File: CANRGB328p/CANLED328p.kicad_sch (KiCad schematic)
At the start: 30 parts, among them J1 Conn_01x06_Socket, J2 Conn_01x03_Socket, J3 AVR-ISP-6, U1 MCP2515-I_SO, U2 TSR_1-2450, U3 MCP2561-E_SN, U4 ATmega328-P, Y1 16 MHz, Y2 8 MHz

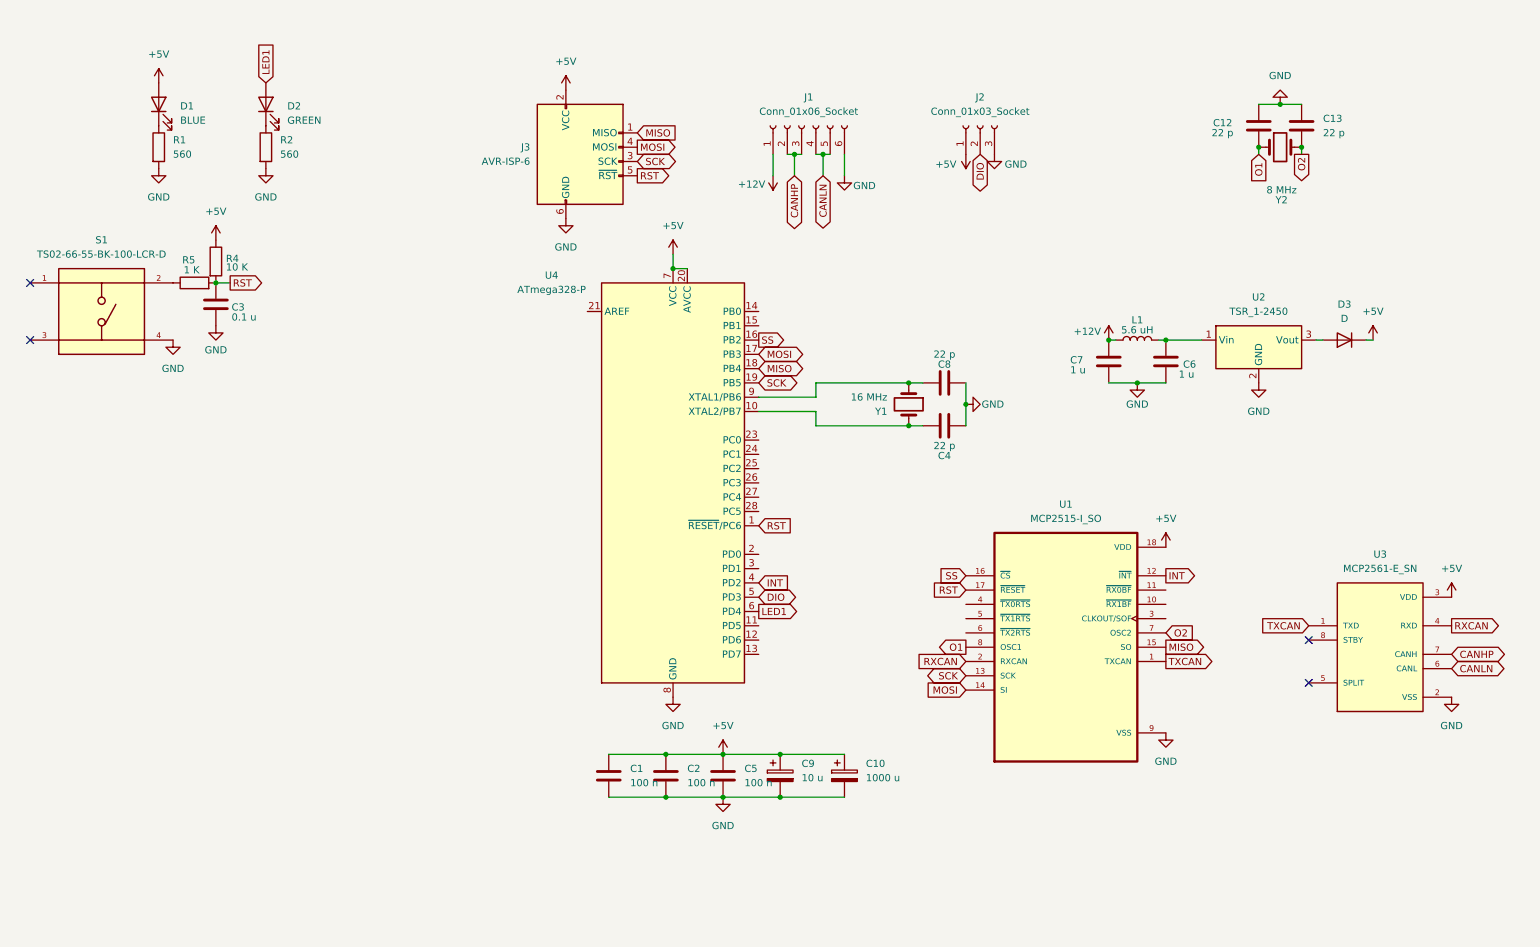
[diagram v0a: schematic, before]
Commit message: Beginning of rev1 redesign - major error fixed
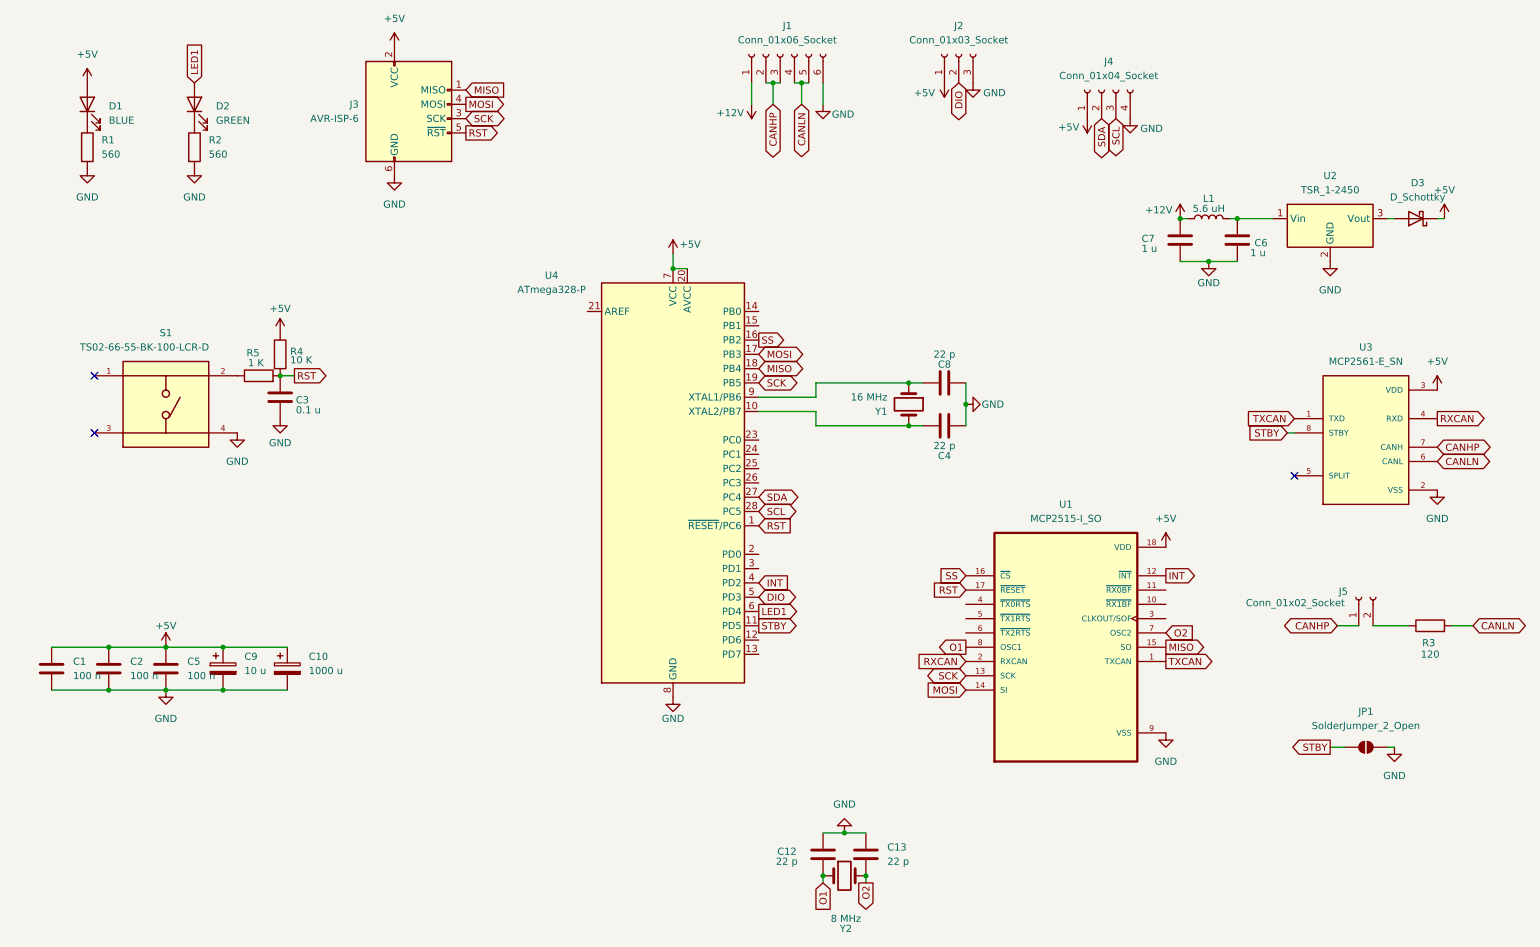
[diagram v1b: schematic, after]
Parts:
- removed D3: D, Diode_THT:D_DO-35_SOD27_P10.16mm_Horizontal, symbol Device:D
- added D3: D_Schottky, symbol Device:D_Schottky
- added J4: Conn_01x04_Socket, symbol Connector:Conn_01x04_Socket
- added J5: Conn_01x02_Socket, symbol Connector:Conn_01x02_Socket
- added JP1: SolderJumper_2_Open, symbol Jumper:SolderJumper_2_Open
- added R3: 120, symbol Device:R
- J1: footprint Connector_PinHeader_2.00mm:PinHeader_1x06_P2.00mm_Vertical -> Connector_PinHeader_1.00mm:PinHeader_1x06_P1.00mm_Vertical
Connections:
- net +5V: now also D3.1 (K), J4.1 (Pin_1)
- net CANHP: now also J5.1 (Pin_1)
- net CANLN: now also R3.2
- net GND: now also J4.4 (Pin_4), JP1.2 (B)
- net at U2.3 (Vout): now also D3.2 (A)
- net STBY: now reaches U4.11 (PD5)
- net STBY: now also U3.8 (STBY), JP1.1 (A)
- net SDA: now reaches U4.27 (PC4)
- net SDA: now also J4.2 (Pin_2)
- net SCL: now reaches U4.28 (PC5)
- net SCL: now also J4.3 (Pin_3)
- new net: J5.2 (Pin_2), R3.1
- no-connect marks 4 -> 3
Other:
- moved on the sheet: C1, C10, C12, C13, C2, C3, C5, C6, C7, C9, D1, D2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
